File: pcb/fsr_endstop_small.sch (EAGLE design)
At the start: 33 parts, among them U1 ATTINY461

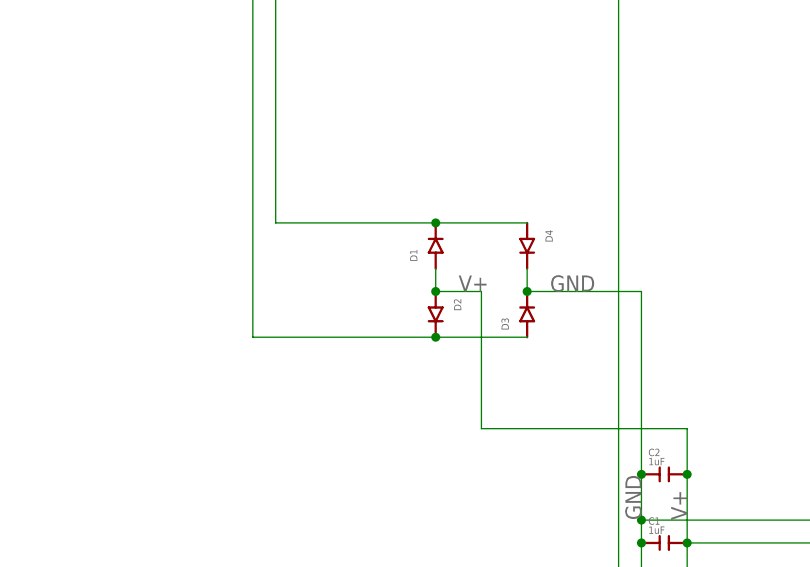
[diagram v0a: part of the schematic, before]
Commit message: Reverse polarity of diodes
Diodes were backwards in the schematic for the bridge rectifier.
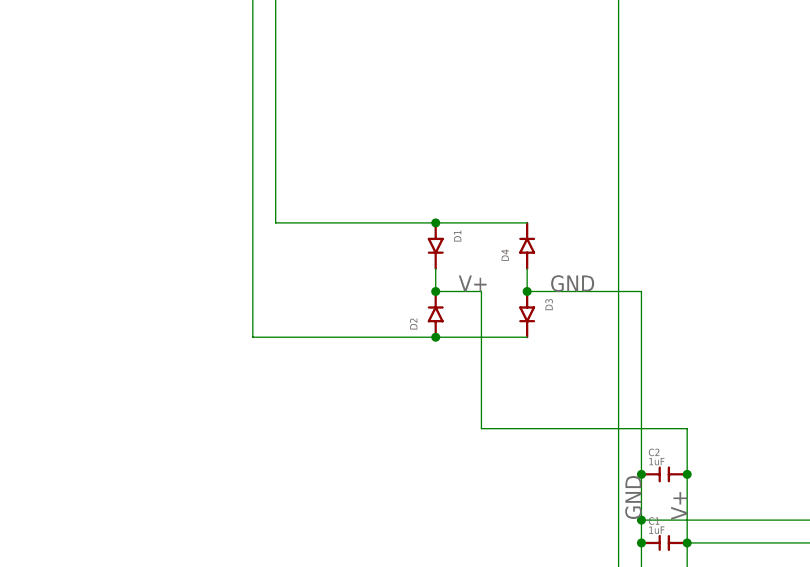
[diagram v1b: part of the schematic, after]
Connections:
- net GND: now also D3.+, D4.+; no longer D3.-, D4.-
- net N$3: now also D2.+, D3.-; no longer D2.-, D3.+
- net N$4: now also D1.+, D4.-; no longer D1.-, D4.+
- net V+: now also D1.-, D2.-; no longer D1.+, D2.+
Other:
- moved on the sheet: D1, D2, D3, D4
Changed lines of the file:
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@@
 <instance part="FSR3A" gate="G$1" x="129.54" y="88.9" rot="R270"/>
 <instance part="AVR1" gate="G$1" x="50.8" y="10.16" rot="R90"/>
-<instance part="D1" gate="G$1" x="20.32" y="111.76" rot="R90"/>
-<instance part="D2" gate="G$1" x="20.32" y="104.14" rot="R270"/>
-<instance part="D3" gate="G$1" x="30.48" y="104.14" rot="R90"/>
-<instance part="D4" gate="G$1" x="30.48" y="111.76" rot="R270"/>
+<instance part="D1" gate="G$1" x="20.32" y="111.76" rot="R270"/>
+<instance part="D2" gate="G$1" x="20.32" y="104.14" rot="R90"/>
+<instance part="D3" gate="G$1" x="30.48" y="104.14" rot="R270"/>
+<instance part="D4" gate="G$1" x="30.48" y="111.76" rot="R90"/>
 <instance part="C1" gate="G$1" x="45.72" y="78.74"/>
 <instance part="LED1" gate="G$1" x="190.5" y="43.18"/>
@@
 <net name="N$3" class="0">
 <segment>
-<pinref part="D3" gate="G$1" pin="+"/>
-<pinref part="D2" gate="G$1" pin="-"/>
-<wire x1="30.48" y1="101.6" x2="20.32" y2="101.6" width="0.1524" layer="91"/>
-<wire x1="20.32" y1="101.6" x2="0" y2="101.6" width="0.1524" layer="91"/>
 <wire x1="0" y1="101.6" x2="0" y2="152.4" width="0.1524" layer="91"/>
-<junction x="20.32" y="101.6"/>
 <pinref part="-/+" gate="G$1" pin="P$1"/>
 <wire x1="0" y1="152.4" x2="-12.7" y2="152.4" width="0.1524" layer="91"/>
+<pinref part="D2" gate="G$1" pin="+"/>
+<wire x1="0" y1="101.6" x2="20.32" y2="101.6" width="0.1524" layer="91"/>
+<pinref part="D3" gate="G$1" pin="-"/>
+<wire x1="20.32" y1="101.6" x2="30.48" y2="101.6" width="0.1524" layer="91"/>
+<junction x="20.32" y="101.6"/>
 </segment>
 </net>
@@
 <wire x1="-12.7" y1="162.56" x2="2.54" y2="162.56" width="0.1524" layer="91"/>
 <wire x1="2.54" y1="162.56" x2="2.54" y2="114.3" width="0.1524" layer="91"/>
-<pinref part="D1" gate="G$1" pin="-"/>
+<pinref part="D1" gate="G$1" pin="+"/>
 <wire x1="2.54" y1="114.3" x2="20.32" y2="114.3" width="0.1524" layer="91"/>
-<pinref part="D4" gate="G$1" pin="+"/>
+<pinref part="D4" gate="G$1" pin="-"/>
 <wire x1="20.32" y1="114.3" x2="30.48" y2="114.3" width="0.1524" layer="91"/>
 <junction x="20.32" y="114.3"/>
@@
 <net name="V+" class="0">
 <segment>
-<pinref part="D2" gate="G$1" pin="+"/>
-<pinref part="D1" gate="G$1" pin="+"/>
-<wire x1="20.32" y1="106.68" x2="20.32" y2="109.22" width="0.1524" layer="91"/>
-<wire x1="20.32" y1="106.68" x2="25.4" y2="106.68" width="0.1524" layer="91"/>
-<junction x="20.32" y="106.68"/>
 <wire x1="25.4" y1="106.68" x2="25.4" y2="91.44" width="0.1524" layer="91"/>
 <pinref part="U1" gate="G$1" pin="15_AVCC"/>
@@
 <pinref part="C2" gate="G$1" pin="P$2"/>
 <junction x="48.26" y="86.36"/>
+<pinref part="D1" gate="G$1" pin="-"/>
+<pinref part="D2" gate="G$1" pin="-"/>
+<wire x1="20.32" y1="109.22" x2="20.32" y2="106.68" width="0.1524" layer="91"/>
+<wire x1="20.32" y1="106.68" x2="25.4" y2="106.68" width="0.1524" layer="91"/>
+<junction x="20.32" y="106.68"/>
 </segment>
 </net>
 <net name="GND" class="0">
 <segment>
-<pinref part="D4" gate="G$1" pin="-"/>
-<pinref part="D3" gate="G$1" pin="-"/>
-<wire x1="30.48" y1="109.22" x2="30.48" y2="106.68" width="0.1524" layer="91"/>
 <pinref part="C1" gate="G$1" pin="P$1"/>
 <wire x1="43.18" y1="78.74" x2="43.18" y2="58.42" width="0.1524" layer="91"/>
@@
 <wire x1="43.18" y1="33.02" x2="43.18" y2="58.42" width="0.1524" layer="91"/>
 <junction x="43.18" y="58.42"/>
-<wire x1="30.48" y1="106.68" x2="43.18" y2="106.68" width="0.1524" layer="91"/>
 <wire x1="43.18" y1="106.68" x2="43.18" y2="86.36" width="0.1524" layer="91"/>
-<junction x="30.48" y="106.68"/>
 <junction x="43.18" y="78.74"/>
 <label x="43.18" y="81.28" size="1.778" layer="95" rot="R90"/>
@@
 <pinref part="C2" gate="G$1" pin="P$1"/>
 <junction x="43.18" y="86.36"/>
+<pinref part="D4" gate="G$1" pin="+"/>
+<pinref part="D3" gate="G$1" pin="+"/>
+<wire x1="30.48" y1="109.22" x2="30.48" y2="106.68" width="0.1524" layer="91"/>
+<wire x1="30.48" y1="106.68" x2="43.18" y2="106.68" width="0.1524" layer="91"/>
+<junction x="30.48" y="106.68"/>
 </segment>
 </net>

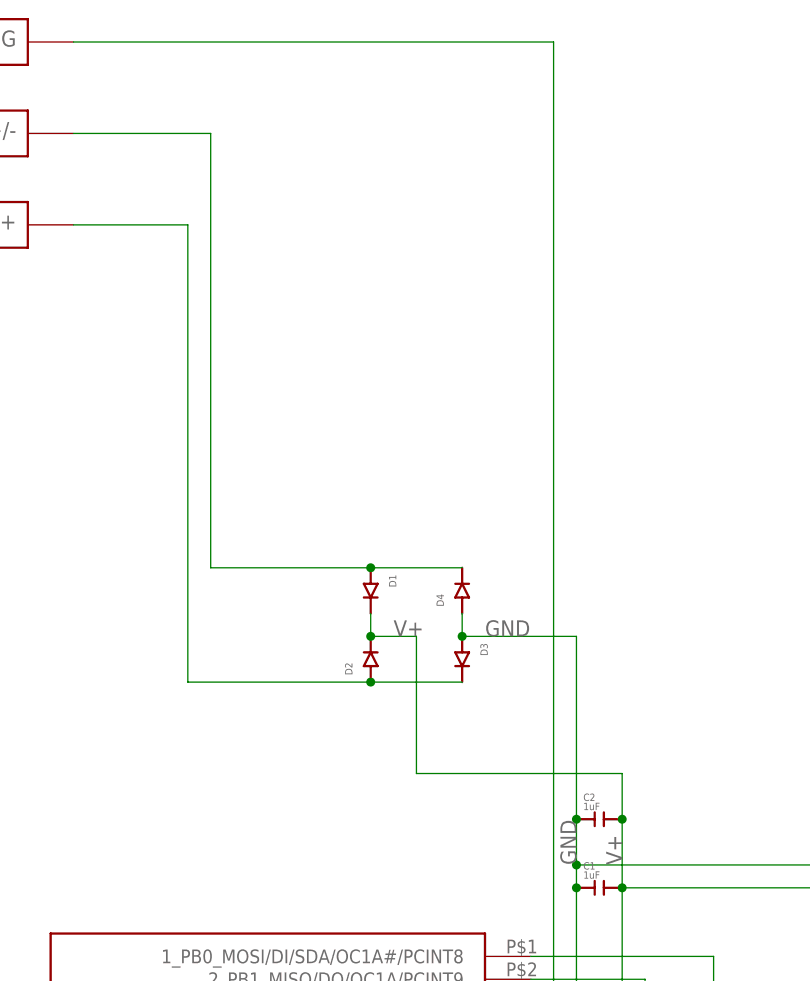
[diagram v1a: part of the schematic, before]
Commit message: Replaced the discrete diodes with a bridge rectifier chip for easier hand soldering.
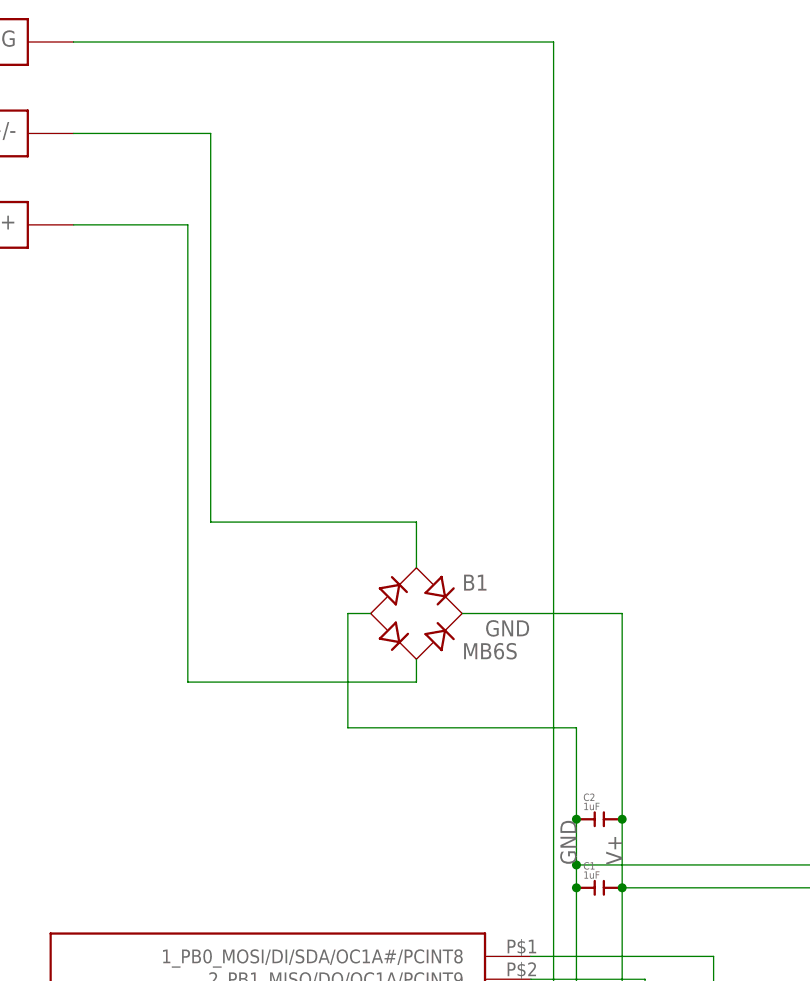
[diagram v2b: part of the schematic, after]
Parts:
- removed D1, D2, D3, D4: (no value), _sg_lib:DIODE0603
- added B1: MB6S, rectifier:MB6S
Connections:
- net GND: now also B1.-; no longer D3.+, D4.+
- net N$3: now also B1.AC2; no longer D2.+, D3.-
- net N$4: now also B1.AC1; no longer D1.+, D4.-
- net V+: now also B1.+; no longer D1.-, D2.-
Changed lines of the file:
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@@
 <?xml version="1.0" encoding="utf-8"?>
 <!DOCTYPE eagle SYSTEM "eagle.dtd">
-<eagle version="6.4">
+<eagle version="6.5.0">
 <drawing>
 <settings>
@@
 <part name="FSR3A" library="_sg_lib" deviceset="PIN" device="1.2MM"/>
 <part name="AVR1" library="_sg_misc" deviceset="AVR6" device=""/>
-<part name="D1" library="_sg_lib" deviceset="DIODE0603" device=""/>
-<part name="D2" library="_sg_lib" deviceset="DIODE0603" device=""/>
-<part name="D3" library="_sg_lib" deviceset="DIODE0603" device=""/>
-<part name="D4" library="_sg_lib" deviceset="DIODE0603" device=""/>
 <part name="C1" library="_sg_lib" deviceset="CAP0603" device="" value="1uF"/>
 <part name="LED1" library="_sg_lib" deviceset="LED0603" device=""/>
@@
 <part name="VCC" library="_sg_lib" deviceset="PIN" device="1.2MM"/>
 <part name="C2" library="_sg_lib" deviceset="CAP0603" device="" value="1uF"/>
+<part name="B1" library="rectifier" deviceset="MB*S" device="" technology="6"/>
 </parts>
 <sheets>
@@
 <instance part="FSR3A" gate="G$1" x="129.54" y="88.9" rot="R270"/>
 <instance part="AVR1" gate="G$1" x="50.8" y="10.16" rot="R90"/>
-<instance part="D1" gate="G$1" x="20.32" y="111.76" rot="R270"/>
-<instance part="D2" gate="G$1" x="20.32" y="104.14" rot="R90"/>
-<instance part="D3" gate="G$1" x="30.48" y="104.14" rot="R270"/>
-<instance part="D4" gate="G$1" x="30.48" y="111.76" rot="R90"/>
 <instance part="C1" gate="G$1" x="45.72" y="78.74"/>
 <instance part="LED1" gate="G$1" x="190.5" y="43.18"/>
@@
 <instance part="VCC" gate="G$1" x="142.24" y="68.58" rot="R270"/>
 <instance part="C2" gate="G$1" x="45.72" y="86.36"/>
+<instance part="B1" gate="G$1" x="25.4" y="109.22"/>
 </instances>
 <busses>
@@
 <pinref part="-/+" gate="G$1" pin="P$1"/>
 <wire x1="0" y1="152.4" x2="-12.7" y2="152.4" width="0.1524" layer="91"/>
-<pinref part="D2" gate="G$1" pin="+"/>
-<wire x1="0" y1="101.6" x2="20.32" y2="101.6" width="0.1524" layer="91"/>
-<pinref part="D3" gate="G$1" pin="-"/>
-<wire x1="20.32" y1="101.6" x2="30.48" y2="101.6" width="0.1524" layer="91"/>
-<junction x="20.32" y="101.6"/>
+<pinref part="B1" gate="G$1" pin="AC2"/>
+<wire x1="25.4" y1="104.14" x2="25.4" y2="101.6" width="0.1524" layer="91"/>
+<wire x1="25.4" y1="101.6" x2="0" y2="101.6" width="0.1524" layer="91"/>
 </segment>
 </net>
@@
 <pinref part="+/-" gate="G$1" pin="P$1"/>
 <wire x1="-12.7" y1="162.56" x2="2.54" y2="162.56" width="0.1524" layer="91"/>
-<wire x1="2.54" y1="162.56" x2="2.54" y2="114.3" width="0.1524" layer="91"/>
-<pinref part="D1" gate="G$1" pin="+"/>
-<wire x1="2.54" y1="114.3" x2="20.32" y2="114.3" width="0.1524" layer="91"/>
-<pinref part="D4" gate="G$1" pin="-"/>
-<wire x1="20.32" y1="114.3" x2="30.48" y2="114.3" width="0.1524" layer="91"/>
-<junction x="20.32" y="114.3"/>
+<wire x1="2.54" y1="162.56" x2="2.54" y2="119.38" width="0.1524" layer="91"/>
+<wire x1="2.54" y1="119.38" x2="25.4" y2="119.38" width="0.1524" layer="91"/>
+<pinref part="B1" gate="G$1" pin="AC1"/>
+<wire x1="25.4" y1="119.38" x2="25.4" y2="114.3" width="0.1524" layer="91"/>
 </segment>
 </net>
 <net name="V+" class="0">
 <segment>
-<wire x1="25.4" y1="106.68" x2="25.4" y2="91.44" width="0.1524" layer="91"/>
 <pinref part="U1" gate="G$1" pin="15_AVCC"/>
 <pinref part="C1" gate="G$1" pin="P$2"/>
@@
 <wire x1="38.1" y1="60.96" x2="48.26" y2="60.96" width="0.1524" layer="91"/>
 <junction x="48.26" y="60.96"/>
-<wire x1="25.4" y1="91.44" x2="48.26" y2="91.44" width="0.1524" layer="91"/>
-<wire x1="48.26" y1="91.44" x2="48.26" y2="86.36" width="0.1524" layer="91"/>
 <junction x="48.26" y="78.74"/>
 <label x="48.26" y="81.28" size="1.778" layer="95" rot="R90"/>
-<label x="22.86" y="106.68" size="1.778" layer="95"/>
 <wire x1="48.26" y1="86.36" x2="48.26" y2="78.74" width="0.1524" layer="91"/>
 <wire x1="48.26" y1="35.56" x2="48.26" y2="20.32" width="0.1524" layer="91"/>
@@
 <pinref part="C2" gate="G$1" pin="P$2"/>
 <junction x="48.26" y="86.36"/>
-<pinref part="D1" gate="G$1" pin="-"/>
-<pinref part="D2" gate="G$1" pin="-"/>
-<wire x1="20.32" y1="109.22" x2="20.32" y2="106.68" width="0.1524" layer="91"/>
-<wire x1="20.32" y1="106.68" x2="25.4" y2="106.68" width="0.1524" layer="91"/>
-<junction x="20.32" y="106.68"/>
+<wire x1="48.26" y1="86.36" x2="48.26" y2="109.22" width="0.1524" layer="91"/>
+<pinref part="B1" gate="G$1" pin="+"/>
+<wire x1="48.26" y1="109.22" x2="30.48" y2="109.22" width="0.1524" layer="91"/>
 </segment>
 </net>
@@
 <wire x1="43.18" y1="33.02" x2="43.18" y2="58.42" width="0.1524" layer="91"/>
 <junction x="43.18" y="58.42"/>
-<wire x1="43.18" y1="106.68" x2="43.18" y2="86.36" width="0.1524" layer="91"/>
+<wire x1="43.18" y1="96.52" x2="43.18" y2="86.36" width="0.1524" layer="91"/>
 <junction x="43.18" y="78.74"/>
 <label x="43.18" y="81.28" size="1.778" layer="95" rot="R90"/>
@@
 <pinref part="C2" gate="G$1" pin="P$1"/>
 <junction x="43.18" y="86.36"/>
-<pinref part="D4" gate="G$1" pin="+"/>
-<pinref part="D3" gate="G$1" pin="+"/>
-<wire x1="30.48" y1="109.22" x2="30.48" y2="106.68" width="0.1524" layer="91"/>
-<wire x1="30.48" y1="106.68" x2="43.18" y2="106.68" width="0.1524" layer="91"/>
-<junction x="30.48" y="106.68"/>
-</segment>
-</net>
+<wire x1="43.18" y1="96.52" x2="17.78" y2="96.52" width="0.1524" layer="91"/>
+<wire x1="17.78" y1="96.52" x2="17.78" y2="109.22" width="0.1524" layer="91"/>
+<pinref part="B1" gate="G$1" pin="-"/>
+<wire x1="17.78" y1="109.22" x2="20.32" y2="109.22" width="0.1524" layer="91"/>
+</segment>
+</net>
